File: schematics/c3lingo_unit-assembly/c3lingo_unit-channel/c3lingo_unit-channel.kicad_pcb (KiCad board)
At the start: 2 copper layers, 162 x 87 mm, 92 parts, among them J1 Headphone 1, J2 Mic 1, J3 Mix Line-Out, J4 Stage Line-In, J5 PowerSupply, J6 PowerSupply, SW1 Mute_1, SW2 OnAir_1, U1 LM833N, U2 NE5534, U3 LM833N, U4 LM833N, U5 DRV134PA, U7 LM386N-4

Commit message: PCB: Channel strip design
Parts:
- removed C10: 22pF, Capacitor_THT:C_Disc_D5.0mm_W2.5mm_P5.00mm
- removed C11, C12, C15, C16: 100nF, Capacitor_THT:C_Disc_D5.0mm_W2.5mm_P5.00mm
- removed C14: 47pF, Capacitor_THT:C_Disc_D5.0mm_W2.5mm_P5.00mm
- removed C17, C18: 1uF, Capacitor_THT:C_Disc_D5.0mm_W2.5mm_P5.00mm
- removed C27: 220pF, Capacitor_THT:C_Disc_D5.0mm_W2.5mm_P5.00mm
- removed J3: Mix Line-Out, Connector_PinHeader_2.54mm:PinHeader_1x04_P2.54mm_Vertical
- removed J4: Stage Line-In, Connector_PinHeader_2.54mm:PinHeader_1x04_P2.54mm_Vertical
- removed J5, J6: PowerSupply, TerminalBlock_MetzConnect:TerminalBlock_MetzConnect_Type073_RT02603HBLU_1x03_P5.08mm_Horizontal
- removed R12, R13, R14, R16, R19: 22K, Resistor_THT:R_Axial_DIN0207_L6.3mm_D2.5mm_P10.16mm_Horizontal
- removed R17, R18, R21, R23, R3, R8: 10K, Resistor_THT:R_Axial_DIN0207_L6.3mm_D2.5mm_P10.16mm_Horizontal
- removed R20: 47K, Resistor_THT:R_Axial_DIN0207_L6.3mm_D2.5mm_P10.16mm_Horizontal
- removed R4: 3.3K, Resistor_THT:R_Axial_DIN0207_L6.3mm_D2.5mm_P10.16mm_Horizontal
- removed RV1: 100K, Potentiometer_THT:Potentiometer_Vishay_T73XX_Horizontal
- removed SW2: OnAir_1, Connector_PinHeader_2.54mm:PinHeader_1x04_P2.54mm_Vertical
- removed TP1, TP9: Mic1, TestPoint:TestPoint_THTPad_D2.0mm_Drill1.0mm
- removed TP10: Mic2, TestPoint:TestPoint_THTPad_D2.0mm_Drill1.0mm
- removed TP11: Mic3, TestPoint:TestPoint_THTPad_D2.0mm_Drill1.0mm
- removed TP6: MicSum, TestPoint:TestPoint_THTPad_D2.0mm_Drill1.0mm
- removed TP8: Stage, TestPoint:TestPoint_THTPad_D2.0mm_Drill1.0mm
- removed U1, U3, U4: LM833N, Package_DIP:DIP-8_W7.62mm_Socket_LongPads
- removed U5: DRV134PA, Package_DIP:DIP-8_W7.62mm_Socket_LongPads
- added C119: 1uF, Capacitor_THT:CP_Radial_D5.0mm_P2.00mm, B.Cu at (99.8, 151.1)
- added C120: 47uF, Capacitor_THT:CP_Radial_D6.3mm_P2.50mm, B.Cu at (116.8, 123.2)
- added C121: 100nF, Capacitor_THT:C_Disc_D5.0mm_W2.5mm_P5.00mm, B.Cu at (116.9, 153.7)
- added C122: 100nF, Capacitor_THT:C_Disc_D5.0mm_W2.5mm_P5.00mm, B.Cu at (121.9, 135.9)
- added C123: 100nF, Capacitor_THT:C_Disc_D5.0mm_W2.5mm_P5.00mm, B.Cu at (102.9, 127.0)
- added C124: 100nF, Capacitor_THT:C_Disc_D5.0mm_W2.5mm_P5.00mm, B.Cu at (102.9, 101.6)
- added C125: 100nF, Capacitor_THT:C_Disc_D5.0mm_W2.5mm_P5.00mm, B.Cu at (102.9, 76.2)
- added D101: On-Air (rd), LED_THT:LED_D5.0mm, F.Cu at (57.0, 68.5)
- added D106: rd, LED_THT:LED_D5.0mm, F.Cu at (83.0, 128.0)
- added D107: rd, LED_THT:LED_D5.0mm, F.Cu at (83.0, 121.5)
- added D108: rd, LED_THT:LED_D5.0mm, F.Cu at (83.0, 115.0)
- added D109: rd, LED_THT:LED_D5.0mm, F.Cu at (83.0, 108.5)
- added D110: ye, LED_THT:LED_D5.0mm, F.Cu at (83.0, 102.0)
- added D111: ye, LED_THT:LED_D5.0mm, F.Cu at (83.0, 95.5)
- added D112: gn, LED_THT:LED_D5.0mm, F.Cu at (83.0, 89.0)
- added D113: gn, LED_THT:LED_D5.0mm, F.Cu at (83.0, 82.5)
- added D114: gn, LED_THT:LED_D5.0mm, F.Cu at (83.0, 76.0)
- added D115: ye, LED_THT:LED_D5.0mm, F.Cu at (83.0, 69.5)
- added D116: ye, LED_THT:LED_D5.0mm, F.Cu at (83.0, 63.0)
- added D117: rd, LED_THT:LED_D5.0mm, F.Cu at (83.0, 56.5)
- added D118: 1N4148, Diode_THT:D_DO-35_SOD27_P10.16mm_Horizontal, F.Cu at (111.8, 133.3)
- added D119: 1N4148, Diode_THT:D_DO-35_SOD27_P10.16mm_Horizontal, F.Cu at (97.8, 133.3)
- added H301: MountingHole, MountingHole:MountingHole_3.2mm_M3, F.Cu at (53.0, 53.0)
- added H302: MountingHole, MountingHole:MountingHole_3.2mm_M3, F.Cu at (53.0, 167.0)
- added H303: MountingHole, MountingHole:MountingHole_3.2mm_M3, F.Cu at (122.0, 167.0)
- added H305: MountingHole, MountingHole:MountingHole_3.2mm_M3, F.Cu at (53.0, 176.0)
- added H306: MountingHole, MountingHole:MountingHole_3.2mm_M3, F.Cu at (122.0, 176.0)
- added J103: PowerSupply, TerminalBlock_Phoenix:TerminalBlock_Phoenix_PTSM-0,5-4-2.5-H-THR_1x04_P2.50mm_Horizontal, B.Cu at (69.8, 53.3)
- added J104: Inputs, TerminalBlock_Phoenix:TerminalBlock_Phoenix_PTSM-0,5-4-2.5-H-THR_1x04_P2.50mm_Horizontal, B.Cu at (53.3, 151.1)
- added J105: Output, TerminalBlock_Phoenix:TerminalBlock_Phoenix_PTSM-0,5-2-2.5-H-THR_1x02_P2.50mm_Horizontal, B.Cu at (53.3, 108.0)
- added J106: PowerSupply, TerminalBlock_Phoenix:TerminalBlock_Phoenix_PTSM-0,5-4-2.5-H-THR_1x04_P2.50mm_Horizontal, F.Cu at (80.0, 177.2)
- added J107: Interconnect, TerminalBlock_Phoenix:TerminalBlock_Phoenix_PTSM-0,5-3-2.5-H-THR_1x03_P2.50mm_Horizontal, F.Cu at (108.0, 177.2)
- added J108: Interconnect, TerminalBlock_Phoenix:TerminalBlock_Phoenix_PTSM-0,5-3-2.5-H-THR_1x03_P2.50mm_Horizontal, B.Cu at (53.3, 137.2)
- added JP102: GND_JMP, Jumper:SolderJumper-2_P1.3mm_Open_TrianglePad1.0x1.5mm, B.Cu at (76.2, 217.8)
- added R106: 390R, Resistor_THT:R_Axial_DIN0207_L6.3mm_D2.5mm_P10.16mm_Horizontal, F.Cu at (53.3, 61.0)
- added R120: 3.9K, Resistor_THT:R_Axial_DIN0207_L6.3mm_D2.5mm_P10.16mm_Horizontal, F.Cu at (97.8, 138.4)
- added R121: 390R, Resistor_THT:R_Axial_DIN0207_L6.3mm_D2.5mm_P10.16mm_Horizontal, F.Cu at (87.6, 125.7)
- added R122: 390R, Resistor_THT:R_Axial_DIN0207_L6.3mm_D2.5mm_P10.16mm_Horizontal, F.Cu at (87.6, 119.4)
- added R123: 390R, Resistor_THT:R_Axial_DIN0207_L6.3mm_D2.5mm_P10.16mm_Horizontal, F.Cu at (87.6, 113.0)
- added R124: 390R, Resistor_THT:R_Axial_DIN0207_L6.3mm_D2.5mm_P10.16mm_Horizontal, F.Cu at (87.6, 106.7)
- added R125: 390R, Resistor_THT:R_Axial_DIN0207_L6.3mm_D2.5mm_P10.16mm_Horizontal, F.Cu at (87.6, 100.3)
- added R126: 390R, Resistor_THT:R_Axial_DIN0207_L6.3mm_D2.5mm_P10.16mm_Horizontal, F.Cu at (87.6, 94.0)
- added R127: 390R, Resistor_THT:R_Axial_DIN0207_L6.3mm_D2.5mm_P10.16mm_Horizontal, F.Cu at (87.6, 87.6)
- added R128: 390R, Resistor_THT:R_Axial_DIN0207_L6.3mm_D2.5mm_P10.16mm_Horizontal, F.Cu at (87.6, 81.3)
- added R129: 390R, Resistor_THT:R_Axial_DIN0207_L6.3mm_D2.5mm_P10.16mm_Horizontal, F.Cu at (87.6, 74.9)
- added R130: 390R, Resistor_THT:R_Axial_DIN0207_L6.3mm_D2.5mm_P10.16mm_Horizontal, F.Cu at (87.6, 68.6)
- added R131: 390R, Resistor_THT:R_Axial_DIN0207_L6.3mm_D2.5mm_P10.16mm_Horizontal, F.Cu at (87.6, 62.2)
- added R132: 390R, Resistor_THT:R_Axial_DIN0207_L6.3mm_D2.5mm_P10.16mm_Horizontal, F.Cu at (87.6, 55.9)
- added R133: 1K, Resistor_THT:R_Axial_DIN0207_L6.3mm_D2.5mm_P10.16mm_Horizontal, F.Cu at (97.8, 143.5)
- added R134: 68R, Resistor_THT:R_Axial_DIN0207_L6.3mm_D2.5mm_P10.16mm_Horizontal, F.Cu at (113.0, 116.8)
- added R135: 39R, Resistor_THT:R_Axial_DIN0207_L6.3mm_D2.5mm_P10.16mm_Horizontal, F.Cu at (113.0, 111.8)
- added R136: 68R, Resistor_THT:R_Axial_DIN0207_L6.3mm_D2.5mm_P10.16mm_Horizontal, F.Cu at (113.0, 106.7)
- added R137: 100R, Resistor_THT:R_Axial_DIN0207_L6.3mm_D2.5mm_P10.16mm_Horizontal, F.Cu at (113.0, 101.6)
- added R138: 150R, Resistor_THT:R_Axial_DIN0207_L6.3mm_D2.5mm_P10.16mm_Horizontal, F.Cu at (113.0, 96.5)
- added R139: 270R, Resistor_THT:R_Axial_DIN0207_L6.3mm_D2.5mm_P10.16mm_Horizontal, F.Cu at (113.0, 91.4)
- added R140: 390R, Resistor_THT:R_Axial_DIN0207_L6.3mm_D2.5mm_P10.16mm_Horizontal, F.Cu at (113.0, 86.4)
- added R141: 680R, Resistor_THT:R_Axial_DIN0207_L6.3mm_D2.5mm_P10.16mm_Horizontal, F.Cu at (113.0, 81.3)
- added R142: 1K, Resistor_THT:R_Axial_DIN0207_L6.3mm_D2.5mm_P10.16mm_Horizontal, F.Cu at (113.0, 76.2)
- added R143: 1.5K, Resistor_THT:R_Axial_DIN0207_L6.3mm_D2.5mm_P10.16mm_Horizontal, F.Cu at (113.0, 71.1)
- added R144: 2.7K, Resistor_THT:R_Axial_DIN0207_L6.3mm_D2.5mm_P10.16mm_Horizontal, F.Cu at (113.0, 66.0)
- added R145: 3.9K, Resistor_THT:R_Axial_DIN0207_L6.3mm_D2.5mm_P10.16mm_Horizontal, F.Cu at (113.0, 61.0)
- added R146: 2.7K, Resistor_THT:R_Axial_DIN0207_L6.3mm_D2.5mm_P10.16mm_Horizontal, F.Cu at (113.0, 55.9)
- added R147: 100K, Resistor_THT:R_Axial_DIN0207_L6.3mm_D2.5mm_P10.16mm_Horizontal, F.Cu at (113.0, 129.5)
- added REF**: mouse-bite-3mm-6mm, c3lingo_unit-footprints:mouse-bite-3mm-6mm, F.Cu at (113.0, 171.5)
- added REF**: mouse-bite-3mm-6mm, c3lingo_unit-footprints:mouse-bite-3mm-6mm, F.Cu at (58.0, 171.5)
- added RV106: 50K, Potentiometer_THT:Potentiometer_Vishay_T73XX_Horizontal, B.Cu at (105.4, 148.6)
- added SW101: OnAir_X, c3lingo_unit-footprints:SW_APEM_MHPS2273_DPDT, F.Cu at (68.0, 70.0)
- added U102: LM833N, Package_DIP:DIP-8_W7.62mm_Socket_LongPads, B.Cu at (61.0, 119.4)
- added U104: LM833N, Package_DIP:DIP-8_W7.62mm_Socket_LongPads, B.Cu at (123.2, 141.0)
- added U105: LM339, Package_DIP:DIP-14_W7.62mm_Socket_LongPads, B.Cu at (101.6, 121.9)
- added U106: LM339, Package_DIP:DIP-14_W7.62mm_Socket_LongPads, B.Cu at (101.6, 96.5)
- added U107: LM339, Package_DIP:DIP-14_W7.62mm_Socket_LongPads, B.Cu at (101.6, 71.1)
- C101: renamed from C1; footprint Capacitor_THT:CP_Radial_D10.0mm_P5.00mm -> Capacitor_THT:CP_Radial_D6.3mm_P2.50mm
- C102: renamed from C21; footprint Capacitor_THT:CP_Radial_D10.0mm_P5.00mm -> Capacitor_THT:CP_Radial_D6.3mm_P2.50mm
- C107: renamed from C13; value 1uF -> 1uF/ 63V
- C108: renamed from C23; footprint Capacitor_THT:CP_Radial_D10.0mm_P5.00mm -> Capacitor_THT:CP_Radial_D6.3mm_P2.50mm
- C110: renamed from C24; value 220uF -> 220uF lowESR
- C111: renamed from C19; value 100uF -> 100uF/ 63V
- C113: renamed from C20; value 1uF -> 1uF/ 63V
- C116: renamed from C4; moved to B.Cu
- C117: renamed from C5; moved to B.Cu
- C118: renamed from C9; footprint Capacitor_THT:CP_Radial_D10.0mm_P5.00mm -> Capacitor_THT:CP_Radial_D6.3mm_P2.50mm
- J101: renamed from J2; value Mic 1 -> Mic X In; footprint Connector_PinHeader_2.54mm:PinHeader_1x04_P2.54mm_Vertical -> Connector_Audio:Jack_XLR_Neutrik_NC3FAAH2_Horizontal
- J102: renamed from J1; value Headphone 1 -> Headphone X; footprint Connector_PinHeader_2.54mm:PinHeader_1x04_P2.54mm_Vertical -> Connector_Audio:Jack_6.35mm_Neutrik_NMJ6HFD2_Horizontal
- R105: renamed from R26; value 270R -> 56R
- R110: renamed from R6; value 1.5K -> 330R
- R112: renamed from R7; value 470R -> 820R
- RV101: renamed from RV13; footprint JBeyerstedt-Library:Potentiometer_Alps_RK11K_Single_Horizontal -> c3lingo_unit-footprints:Potentiometer_Alps_RK09K_Double_Vertical
- RV102: renamed from RV11; value 50K log. -> 10K log.; footprint JBeyerstedt-Library:Potentiometer_Alps_RK11K_Single_Horizontal -> Potentiometer_THT:Potentiometer_Alps_RK09K_Single_Vertical
- RV103: renamed from RV14; footprint JBeyerstedt-Library:Potentiometer_Alps_RK11K_Single_Horizontal -> c3lingo_unit-footprints:Potentiometer_Alps_RK09K_Double_Vertical
- RV104: renamed from RV19; footprint JBeyerstedt-Library:Potentiometer_Alps_RK11K_Single_Horizontal -> Potentiometer_THT:Potentiometer_Alps_RK09K_Single_Horizontal
- RV105: renamed from RV15; footprint Potentiometer_THT:Potentiometer_Alps_RK09L_Double_Horizontal -> c3lingo_unit-footprints:Potentiometer_Alps_RK09K_Double_Vertical
- SW302: renamed from SW1; value Mute_1 -> Mute_X; moved to B.Cu
- TP102: renamed from TP3; value Mic1 -> MicX
- TP103: renamed from TP4; value Mic2 -> MicA
- TP104: renamed from TP5; value Mic3 -> MicB
- moved R118 217.3 mm to (108.0, 221.6), turned to 90 degrees
- moved RV104 213.4 mm to (111.5, 229.5), turned to 270 degrees
- moved R111 213.0 mm to (80.0, 210.2), turned to 180 degrees
- moved R107 212.9 mm to (62.2, 210.2), turned to 180 degrees
- moved D104 211.7 mm to (53.3, 206.4), turned to 90 degrees
- moved J102 202.8 mm to (100.0, 216.0), turned to 270 degrees
- moved C111 201.7 mm to (66.0, 206.4), turned to 90 degrees
- moved D105 197.1 mm to (55.9, 196.2), turned to 270 degrees
- moved D102 193.7 mm to (58.4, 188.6), turned to 90 degrees
- moved C107 192.3 mm to (64.8, 188.6)
- moved C113 191.9 mm to (59.7, 196.2)
- moved J101 191.1 mm to (68.8, 220.4), turned to 270 degrees
- moved D103 187.8 mm to (61.0, 178.4), turned to 270 degrees
- moved C114 180.9 mm to (114.3, 221.6), turned to 90 degrees
- moved R113 176.4 mm to (120.7, 211.4), turned to 270 degrees
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- renumbered C3 to C103, C2 to C104, C22 to C105, C25 to C106, C6 to C109, C26 to C112, C7 to C114, C8 to C115, D2 to D102, D1 to D103, D3 to D104, D4 to D105, R28 to R101, R9 to R102, R1 to R103, R2 to R104, R15 to R107, R29 to R108, R5 to R109, R22 to R111, R24 to R113, R10 to R114, R11 to R115, R25 to R116, R30 to R117, R27 to R118, R31 to R119, TP2 to TP101, U2 to U101, U7 to U103
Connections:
- net Mic1 renamed /PreampOut
- net Net-(RV15-Pad3) renamed /Monitor_OthersB
- net Net-(RV15-Pad6) renamed /Monitor_OthersA
- net Stage renamed /Monitor_Stage
- C103 pad 1: Net-(C3-Pad1) -> SumOut
- C105 pad 1: GND -> +15V
- C105 pad 2: +15V -> GND
- C107 pad 1: Net-(C13-Pad1) -> Net-(C107-Pad1)
- C109 pad 1: Net-(C6-Pad1) -> Net-(C109-Pad1)
- C109 pad 2: Net-(C6-Pad2) -> MicPreOut
- C110 pad 2: (no net) -> Net-(C110-Pad2)
- C111 pad 1: +15V -> V_Phant
- C113 pad 1: Net-(C20-Pad1) -> Net-(C113-Pad1)
- J101 pad 2: Net-(C13-Pad1) -> Net-(C107-Pad1)
- J101 pad 3: Net-(C20-Pad1) -> Net-(C113-Pad1)
- R102 pad 1: Net-(C3-Pad1) -> SumOut
- R103 pad 1: Net-(R1-Pad1) -> Net-(R103-Pad1)
- R104 pad 1: Net-(C6-Pad1) -> Net-(R103-Pad1)
- R104 pad 2: Net-(R1-Pad1) -> Net-(C109-Pad1)
- R107 pad 1: Net-(C13-Pad1) -> V_Phant
- R107 pad 2: +15V -> Net-(C107-Pad1)
- R109 pad 1: Net-(R1-Pad1) -> Net-(R103-Pad1)
- R110 pad 2: Net-(C6-Pad2) -> MicGainIn
- R111 pad 1: +15V -> Net-(C113-Pad1)
- R111 pad 2: Net-(C20-Pad1) -> V_Phant
- R112 pad 1: GND -> MicPreOut
- R112 pad 2: Net-(C6-Pad2) -> GND
- R113 pad 1: Net-(C3-Pad1) -> AmpIn
- U101 pad 2: Net-(R1-Pad1) -> Net-(R103-Pad1)
- U101 pad 6: Net-(C6-Pad1) -> Net-(C109-Pad1)
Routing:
- net Net-(C120-Pad1): track 0.00 -> 157.6 mm
- net V_LED: track 0.00 -> 134.6 mm
- net +15V: track 439.5 -> 521.3 mm, vias 1 -> 2
- net Net-(C10-Pad1): track 70.0 -> 0.00 mm
- net Net-(C103-Pad2): track 104.6 -> 39.2 mm, vias 2 -> 0
- net /Monitor_OthersB: track 8.30 -> 68.8 mm
- net /Monitor_OthersA: track 10.5 -> 65.1 mm
- net /PreampOut: track 126.4 -> 179.6 mm, vias 0 -> 1
- net AmpIn: track 0.00 -> 46.9 mm
- net Net-(C3-Pad1): track 46.5 -> 0.00 mm
- net Net-(C107-Pad1): track 0.00 -> 46.2 mm
- net Net-(J4-Pad2): track 43.6 -> 0.00 mm
- net V_Phant: track 0.00 -> 43.5 mm
- net Net-(JP3-Pad3): track 43.3 -> 0.00 mm
- net Net-(J4-Pad3): track 42.2 -> 0.00 mm
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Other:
- board size 162 x 87 mm -> 75 x 183 mm
- board text added: "Gnd +15V -15V V_LED"
- board text added: "Gnd +15V -15V V_Phant"
- board text added: "Gnd Mic X"
- board text added: "Gnd Stage Mic A Mic B"
- board text added: "Gnd Sum In Pre Out"
- board text added: "Gnd Sum Out Mic In"
- board text added: "Mic Gain + Muting"
- board text added: "Mic Preamp +Ph-Pwr"
- board text added: "Others Vol"
- board text added: "Own Vol"
- board text added: "Stage Vol"
- board text added: "c3lingo Interpreter Unit v0.2 2021-05-30 Jannik Beyerstedt (jtbx)"
- board text removed: "Gain+ LP-Filter"
- board text removed: "Gnd,2/T,3/R,1/S"
- board text removed: "Gnd,3,2,1"
- board text removed: "Line Driver"
- board text removed: "Line Input INA134"
- board text removed: "Line Input LM833"
- board text removed: "Mic Gain"
- board text removed: "Mic Preamp"
- board text removed: "Mic1"
- board text removed: "Mic1 In"
- board text removed: "Mic1 Line"
- board text removed: "Mic2 In"
- board text removed: "Mic2,3 Line"
- board text removed: "Mic3 In"
- board text removed: "Mics Sum"
- board text removed: "Mics Summing"
- board text removed: "Mix Line-Out"
- board text removed: "Others"
- board text removed: "Stage"
- board text removed: "Stage Line"
- board text removed: "TRS,GND"
- board text removed: "Trim Pot Only"
- board text removed: "c3lingo Interpreter Unit v0.1 2020-11-12 Jannik Beyerstedt"

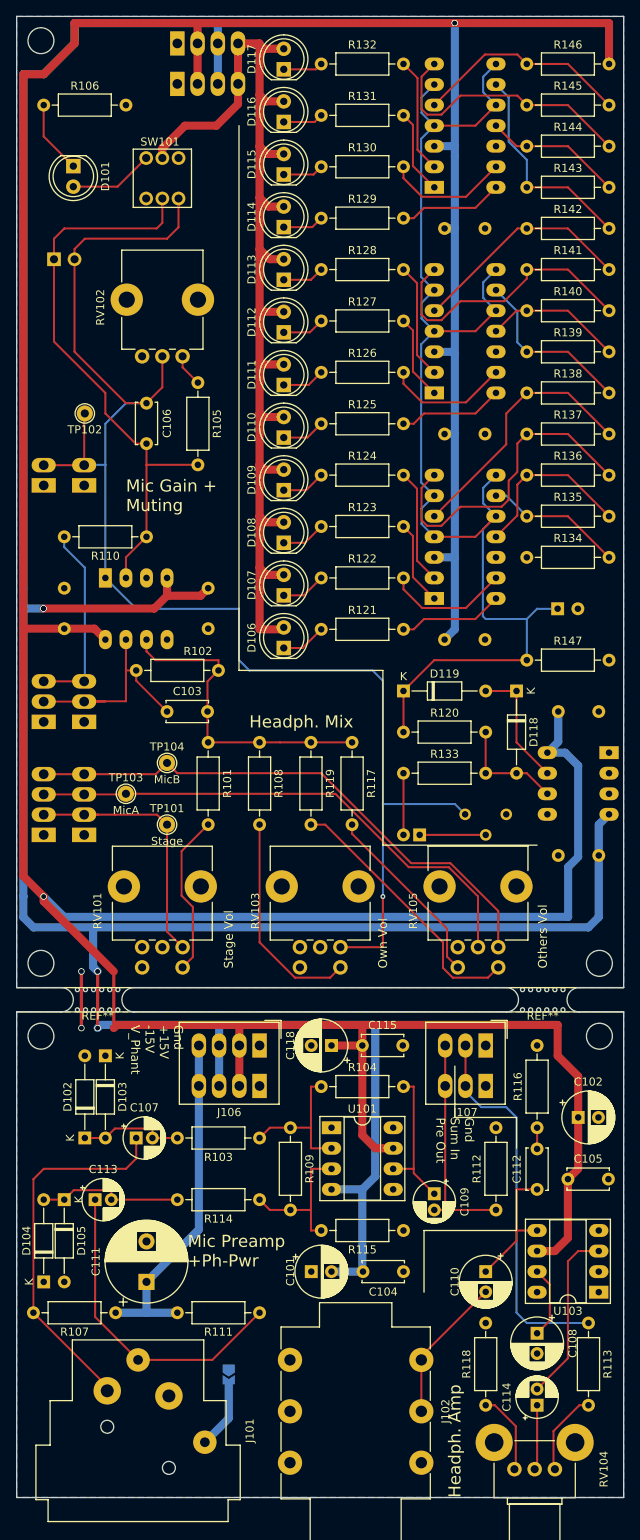
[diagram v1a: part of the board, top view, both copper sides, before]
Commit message: Upgrade project to KiCad 6
Item annotations were re-generated as there were duplicate items otherwise somehow. This means, that some item numbers have changed!
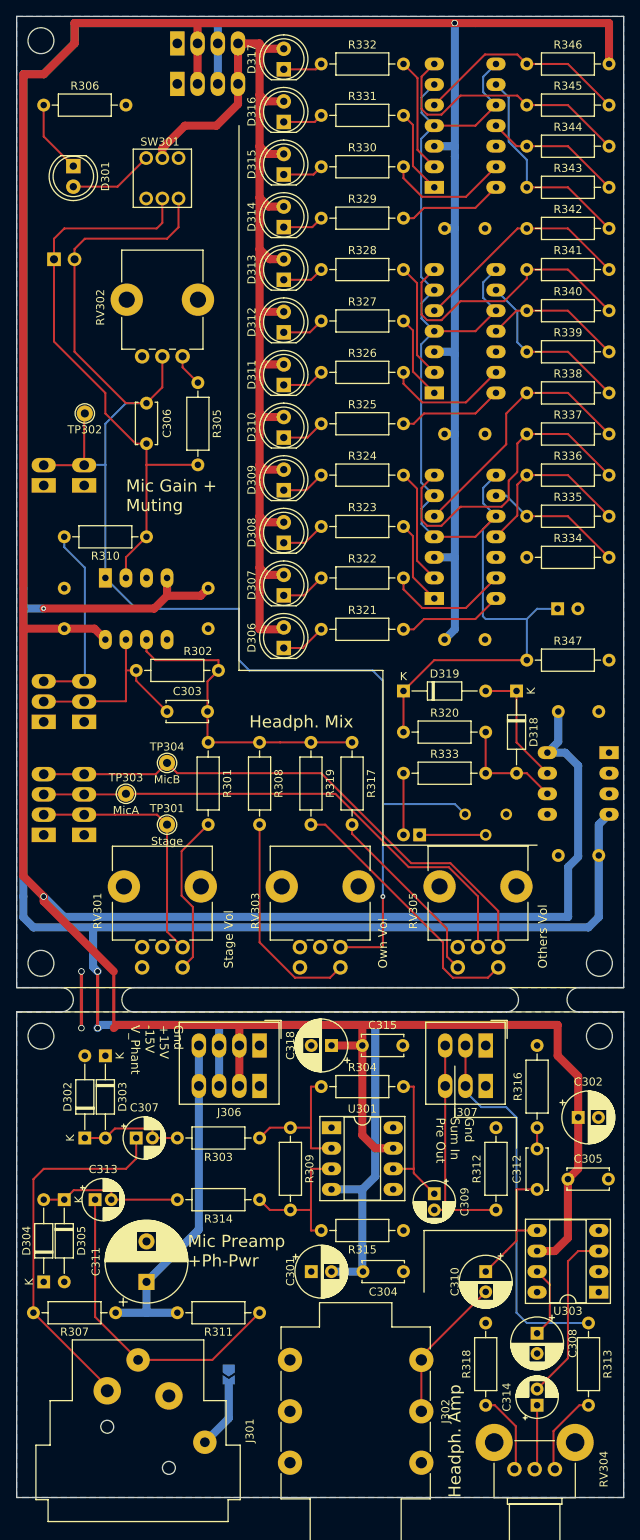
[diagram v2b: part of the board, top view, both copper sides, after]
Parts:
- removed REF** (x2): mouse-bite-3mm-6mm, c3lingo_unit-footprints:mouse-bite-3mm-6mm
- C307: renamed from C107; value 1uF/ 63V -> 1uF/ 63V lowESR
- C313: renamed from C113; value 1uF/ 63V -> 1uF/ 63V lowESR
- R307: renamed from R107; value 680R 1% -> 6.8K 1%
- R311: renamed from R111; value 680R 1% -> 6.8K 1%
- R320: renamed from R120; value 3.9K -> 15K
- renumbered C101 to C301, C102 to C302, C103 to C303, C104 to C304, C105 to C305, C106 to C306, C108 to C308, C109 to C309, C110 to C310, C111 to C311, C112 to C312, C114 to C314, C115 to C315, C116 to C316, C117 to C317, C118 to C318, C119 to C319, C120 to C320, C121 to C321, C122 to C322, C123 to C323, C124 to C324, C125 to C325, D101 to D301, D102 to D302, D103 to D303, D104 to D304, D105 to D305, D106 to D306, D107 to D307, D108 to D308, D109 to D309, D110 to D310, D111 to D311, D112 to D312, D113 to D313, D114 to D314, D115 to D315, D116 to D316, D117 to D317, D118 to D318, D119 to D319, J101 to J301, J102 to J302, J103 to J303, J104 to J304, J105 to J305, J106 to J306, J107 to J307, J108 to J308, JP102 to JP302, R101 to R301, R102 to R302, R103 to R303, R104 to R304, R105 to R305, R106 to R306, R108 to R308, R109 to R309, R110 to R310, R112 to R312, R113 to R313, R114 to R314, R115 to R315, R116 to R316, R117 to R317, R118 to R318, R119 to R319, R121 to R321, R122 to R322, R123 to R323, R124 to R324, R125 to R325, R126 to R326, R127 to R327, R128 to R328, R129 to R329, R130 to R330, R131 to R331, R132 to R332, R133 to R333, R134 to R334, R135 to R335, R136 to R336, R137 to R337, R138 to R338, R139 to R339, R140 to R340, R141 to R341, R142 to R342, R143 to R343, R144 to R344, R145 to R345, R146 to R346, R147 to R347, RV101 to RV301, RV102 to RV302, RV103 to RV303, RV104 to RV304, RV105 to RV305, RV106 to RV306, SW101 to SW301, TP101 to TP301, TP102 to TP302, TP103 to TP303, TP104 to TP304, U101 to U301, U102 to U302, U103 to U303, U104 to U304, U105 to U305, U106 to U306, U107 to U307
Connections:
- RV302 pad 3: (no net) -> unconnected-(RV302-Pad3)
- SW301 pad 3: (no net) -> unconnected-(SW301-Pad3)
- SW301 pad 4: (no net) -> unconnected-(SW301-Pad4)
- U301 pad 1: (no net) -> unconnected-(U301-Pad1)
- U301 pad 5: (no net) -> unconnected-(U301-Pad5)
- U301 pad 8: (no net) -> unconnected-(U301-Pad8)
- U303 pad 1: (no net) -> unconnected-(U303-Pad1)
- U303 pad 8: (no net) -> unconnected-(U303-Pad8)
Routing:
- net SumOut: track 28.3 -> 25.7 mm
- net /Monitor_Stage: track 33.4 -> 31.7 mm
- net Net-(C307-Pad2): track 13.8 -> 13.1 mm
- net -15V: vias 4 -> 3
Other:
- net class Default removed
- net class Power removed
